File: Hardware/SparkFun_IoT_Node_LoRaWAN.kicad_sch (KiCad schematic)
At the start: 72 parts, among them J1 USB_C_Receptacle, J2 JST_2mm_LiPo, J3 Qwiic_RA, SW1 SMD_4.6x2.8mm_h2.5mm, SW2 SMD_4.6x2.8mm_h2.5mm, U4 W25Q128JVPIM, U5 RT9080-3.3, U6 MCP73831, U7 MAX17048, U8 LM66200, U9 RT9080-3.3

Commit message: v01 schematic updates
Add remaining schematic components
Split schematic into multiple sheets
Still need to define pinouts for RP2350, XBLR, and headers
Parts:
- removed C1, C2, C3, C4, C6, C7: 2.2uF, SparkFun-Capacitor:C_0603_1608Metric, symbol SparkFun-Capacitor:2.2uF_0603_10V_20%
- removed C10, C11, C12, C13, C14, C15, C16, C17, C19, C20, C21, C5, C8, C9: 0.1uF, SparkFun-Capacitor:C_0603_1608Metric, symbol SparkFun-Capacitor:0.1uF_0603_25V_20%
- removed C18, C22: 10uF, SparkFun-Capacitor:C_0603_1608Metric, symbol SparkFun-Capacitor:10uF_0603_6.3V_20%
- removed D1: Yellow, SparkFun-LED:LED_0603_1608Metric, symbol SparkFun-LED:LED_Yellow_0603
- removed D2: WS2812B, SparkFun-LED:WS2812-2020, symbol SparkFun-LED:WS2812B_2020
- removed D3: Red, SparkFun-LED:LED_0603_1608Metric, symbol SparkFun-LED:LED_Red_0603
- removed D4: DT1042-04SO, SparkFun-Semiconductor-Standard:SOT23-6, symbol SparkFun-DiscreteSemi:D_TVS_ESD_USB
- removed J1: USB_C_Receptacle, SparkFun-Connector:USB-C_16, symbol SparkFun-Connector:USB_C_Receptacle
- removed J2: JST_2mm_LiPo, SparkFun-Connector:JST_SMD_2.0mm-2, symbol SparkFun-Connector:Conn_01x02_JST_2mm_LiPo
- removed J3: Qwiic_RA, SparkFun-Connector:JST_SMD_1.0mm-4_RA, symbol SparkFun-Connector:Qwiic_Right_Angle
- removed JP1, JP2, JP4: ~, SparkFun-Jumper:Jumper_2_NC_Trace, symbol SparkFun-Jumper:SolderJumper_2_Bridged
- removed JP3: ~, SparkFun-Jumper:Jumper_3_NC-2_Trace, symbol SparkFun-Jumper:SolderJumper_3_Bridged123
- removed L1: 4.7uH, SparkFun-Coil:1008_2520Metric, symbol SparkFun-Coil:4.7uH_1008_1.4A
- removed R1, R2: 5.1k, SparkFun-Resistor:R_0603_1608Metric, symbol SparkFun-Resistor:5.1k_0603
- removed R10, R9: 2.2k, SparkFun-Resistor:R_0603_1608Metric, symbol SparkFun-Resistor:2.2k_0603
- removed R11, R5, R6, R7: 100k, SparkFun-Resistor:R_0603_1608Metric, symbol SparkFun-Resistor:100k_0603
- removed R12, R14, R16: 10k, SparkFun-Resistor:R_0603_1608Metric, symbol SparkFun-Resistor:10k_0603
- removed R13, R8: 4.7k, SparkFun-Resistor:R_0603_1608Metric, symbol SparkFun-Resistor:4.7k_0603
- removed R15: 1k, SparkFun-Resistor:R_0603_1608Metric, symbol SparkFun-Resistor:1k_0603
- removed R3, R4: 27, SparkFun-Resistor:R_0603_1608Metric, symbol SparkFun-Resistor:27_0603
- removed SW1, SW2: SMD_4.6x2.8mm_h2.5mm, SparkFun-Switch:Push_SMD_4.6x2.8mm, symbol SparkFun-Switch:SPST_Push_SMD_4.6x2.8mm_h2.5mm
- removed U1: ~, RP2350A:RP2350A, symbol RP2350A:RP2350A
- removed U2: ~, RP2350A:APS6404L-3SQR-ZR, symbol RP2350A:APS6404L-3SQR-ZR
- removed U3: ~, SparkFun_IoT_Node_LoRaWAN:XBee_LR, symbol SparkFun_IoT_Node_LoRaWAN:XBee_LR
- removed U4: W25Q128JVPIM, SparkFun-Semiconductor-Standard:WDFN-8_6x5mm-SkinnyCenterPad, symbol SparkFun-IC-Memory:W25Q128JVPIM
- removed U5, U9: RT9080-3.3, SparkFun-Semiconductor-Standard:SOT23-5, symbol SparkFun-Regulator:RT9080-3.3
- removed U6: MCP73831, SparkFun-Semiconductor-Standard:SOT23-5, symbol SparkFun-IC-Power:MCP73831
- removed U7: MAX17048, SparkFun-Semiconductor-Standard:DFN-8, symbol SparkFun-IC-Power:MAX17048
- removed U8: LM66200, SparkFun-Semiconductor-Standard:SOT-583-8, symbol SparkFun-IC-Power:LM66200
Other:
- added sheet Power and Peripherals (power_peripherals.kicad_sch)
- added sheet RP2350 (rp2350.kicad_sch)
- added sheet XBLR (xblr.kicad_sch)
- note removed: "16MB Flash"
- note removed: "8MB PSRAM"
- note removed: "Battery Charger"
- note removed: "Battery Fuel Gauge"
- note removed: "Buttons"
- note removed: "LEDs"
- note removed: "LoRaWAN Module - XBee LR"
- note removed: "Max input voltage: 6V"
- note removed: "PTH Headers"
- note removed: "Peripheral Power Control"
- note removed: "Power Input and Voltage Regulator"
- note removed: "Qwiic Connector"
- note removed: "RP2350"
- note removed: "TODO"
- note removed: "USB-C Connector"

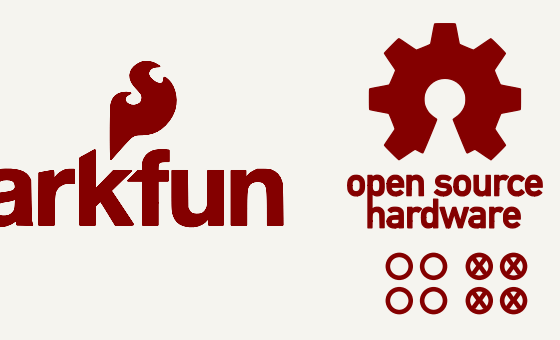
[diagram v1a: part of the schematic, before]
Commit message: Initial board layout
Board outline determined based off selected enclosure
Clusters of components placed and routed
Waiting for feedback before finishing routing
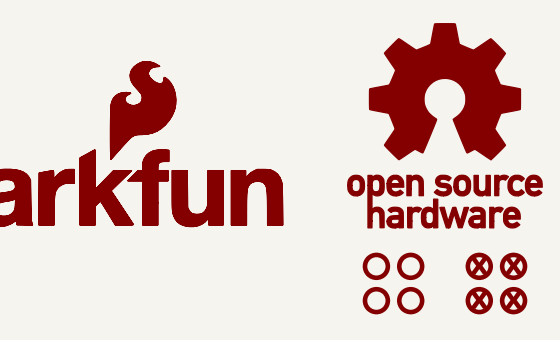
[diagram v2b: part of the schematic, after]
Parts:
- ST1, ST2, ST3, ST4: value Stand_off -> Standoff
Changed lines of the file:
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@@
-	)
-	(symbol
-		(lib_id "SparkFun-Hardware:Standoff")
-		(at 250.19 179.07 0)
-		(unit 1)
-		(exclude_from_sim no)
-		(in_bom yes)
-		(on_board yes)
-		(dnp no)
-		(property "Reference" "ST2"
-			(at 250.19 176.53 0)
-			(effects
-				(font
-					(size 1.27 1.27)
-				)
-				(hide yes)
-			)
-		)
-		(property "Value" "Stand_off"
-			(at 250.19 181.61 0)
-			(effects
-				(font
-					(size 1.27 1.27)
-				)
-				(hide yes)
-			)
-		)
-		(property "Footprint" "SparkFun-Hardware:Standoff"
-			(at 250.19 184.15 0)
-			(effects
-				(font
-					(size 1.27 1.27)
-				)
-				(hide yes)
-			)
-		)
-		(property "Datasheet" "~"
-			(at 250.19 182.88 0)
-			(effects
-				(font
-					(size 1.27 1.27)
-				)
-				(hide yes)
-			)
-		)
-		(property "Description" ""
-			(at 250.19 179.07 0)
-			(effects
-				(font
-					(size 1.27 1.27)
-				)
-				(hide yes)
-			)
-		)
-		(instances
-			(project "SparkFun_Default_KiCad_Setup"
-				(path "/e3dd3ae4-244d-4cba-9cca-5d2abf83f29a"
-					(reference "ST2")
-					(unit 1)
-				)
-			)
-		)
 	)
 	(symbol
@@
 	(symbol
 		(lib_id "SparkFun-Hardware:Standoff")
-		(at 254 179.07 0)
-		(unit 1)
-		(exclude_from_sim no)
-		(in_bom yes)
-		(on_board yes)
-		(dnp no)
+		(at 247.65 175.26 0)
+		(unit 1)
+		(exclude_from_sim no)
+		(in_bom yes)
+		(on_board yes)
+		(dnp no)
+		(fields_autoplaced yes)
 		(property "Reference" "ST4"
-			(at 254 176.53 0)
-			(effects
-				(font
-					(size 1.27 1.27)
-				)
-				(hide yes)
-			)
-		)
-		(property "Value" "Stand_off"
-			(at 254 181.61 0)
+			(at 247.65 172.72 0)
+			(effects
+				(font
+					(size 1.27 1.27)
+				)
+				(hide yes)
+			)
+		)
+		(property "Value" "Standoff"
+			(at 247.65 177.8 0)
 			(effects
 				(font
@@
 		)
 		(property "Footprint" "SparkFun-Hardware:Standoff"
-			(at 254 184.15 0)
-			(effects
-				(font
-					(size 1.27 1.27)
-				)
-				(hide yes)
-			)
-		)
-		(property "Datasheet" "~"
-			(at 254 182.88 0)
-			(effects
-				(font
-					(size 1.27 1.27)
-				)
-				(hide yes)
-			)
-		)
-		(property "Description" ""
-			(at 254 179.07 0)
-			(effects
-				(font
-					(size 1.27 1.27)
-				)
-				(hide yes)
-			)
-		)
-		(instances
-			(project "SparkFun_Default_KiCad_Setup"
+			(at 247.65 180.34 0)
+			(effects
+				(font
+					(size 1.27 1.27)
+				)
+				(hide yes)
+			)
+		)
+		(property "Datasheet" "~"
+			(at 247.65 179.07 0)
+			(effects
+				(font
+					(size 1.27 1.27)
+				)
+				(hide yes)
+			)
+		)
+		(property "Description" "Drill holes for mechanically mounting via screws, standoffs, etc."
+			(at 247.65 175.26 0)
+			(effects
+				(font
+					(size 1.27 1.27)
+				)
+				(hide yes)
+			)
+		)
+		(instances
+			(project "SparkFun_IoT_Node_LoRaWAN"
 				(path "/e3dd3ae4-244d-4cba-9cca-5d2abf83f29a"
 					(reference "ST4")
@@
 	(symbol
 		(lib_id "SparkFun-Hardware:Standoff")
-		(at 250.19 175.26 0)
-		(unit 1)
-		(exclude_from_sim no)
-		(in_bom yes)
-		(on_board yes)
-		(dnp no)
+		(at 247.65 179.07 0)
+		(unit 1)
+		(exclude_from_sim no)
+		(in_bom yes)
+		(on_board yes)
+		(dnp no)
+		(fields_autoplaced yes)
+		(property "Reference" "ST3"
+			(at 247.65 176.53 0)
+			(effects
+				(font
+					(size 1.27 1.27)
+				)
+				(hide yes)
+			)
+		)
+		(property "Value" "Standoff"
+			(at 247.65 181.61 0)
+			(effects
+				(font
+					(size 1.27 1.27)
+				)
+				(hide yes)
+			)
+		)
+		(property "Footprint" "SparkFun-Hardware:Standoff"
+			(at 247.65 184.15 0)
+			(effects
+				(font
+					(size 1.27 1.27)
+				)
+				(hide yes)
+			)
+		)
+		(property "Datasheet" "~"
+			(at 247.65 182.88 0)
+			(effects
+				(font
+					(size 1.27 1.27)
+				)
+				(hide yes)
+			)
+		)
+		(property "Description" "Drill holes for mechanically mounting via screws, standoffs, etc."
+			(at 247.65 179.07 0)
+			(effects
+				(font
+					(size 1.27 1.27)
+				)
+				(hide yes)
+			)
+		)
+		(instances
+			(project "SparkFun_IoT_Node_LoRaWAN"
+				(path "/e3dd3ae4-244d-4cba-9cca-5d2abf83f29a"
+					(reference "ST3")
+					(unit 1)
+				)
+			)
+		)
+	)
+	(symbol
+		(lib_id "SparkFun-Hardware:Standoff")
+		(at 251.46 179.07 0)
+		(unit 1)
+		(exclude_from_sim no)
+		(in_bom yes)
+		(on_board yes)
+		(dnp no)
+		(fields_autoplaced yes)
+		(property "Reference" "ST2"
+			(at 251.46 176.53 0)
+			(effects
+				(font
+					(size 1.27 1.27)
+				)
+				(hide yes)
+			)
+		)
+		(property "Value" "Standoff"
+			(at 251.46 181.61 0)
+			(effects
+				(font
+					(size 1.27 1.27)
+				)
+				(hide yes)
+			)
+		)
+		(property "Footprint" "SparkFun-Hardware:Standoff"
+			(at 251.46 184.15 0)
+			(effects
+				(font
+					(size 1.27 1.27)
+				)
+				(hide yes)
+			)
+		)
+		(property "Datasheet" "~"
+			(at 251.46 182.88 0)
+			(effects
+				(font
+					(size 1.27 1.27)
+				)
+				(hide yes)
+			)
+		)
+		(property "Description" "Drill holes for mechanically mounting via screws, standoffs, etc."
+			(at 251.46 179.07 0)
+			(effects
+				(font
+					(size 1.27 1.27)
+				)
+				(hide yes)
+			)
+		)
+		(instances
+			(project "SparkFun_IoT_Node_LoRaWAN"
+				(path "/e3dd3ae4-244d-4cba-9cca-5d2abf83f29a"
+					(reference "ST2")
+					(unit 1)
+				)
+			)
+		)
+	)
+	(symbol
+		(lib_id "SparkFun-Hardware:Standoff")
+		(at 251.46 175.26 0)
+		(unit 1)
+		(exclude_from_sim no)
+		(in_bom yes)
+		(on_board yes)
+		(dnp no)
+		(fields_autoplaced yes)
 		(property "Reference" "ST1"
-			(at 250.19 172.72 0)
-			(effects
-				(font
-					(size 1.27 1.27)
-				)
-				(hide yes)
-			)
-		)
-		(property "Value" "Stand_off"
-			(at 250.19 177.8 0)
+			(at 251.46 172.72 0)
+			(effects
+				(font
+					(size 1.27 1.27)
+				)
+				(hide yes)
+			)
+		)
+		(property "Value" "Standoff"
+			(at 251.46 177.8 0)
 			(effects
 				(font
@@
 		)
 		(property "Footprint" "SparkFun-Hardware:Standoff"
-			(at 250.19 180.34 0)
-			(effects
-				(font
-					(size 1.27 1.27)
-				)
-				(hide yes)
-			)
-		)
-		(property "Datasheet" "~"
-			(at 250.19 179.07 0)
-			(effects
-				(font
-					(size 1.27 1.27)
-				)
-				(hide yes)
-			)
-		)
-		(property "Description" ""
-			(at 250.19 175.26 0)
-			(effects
-				(font
-					(size 1.27 1.27)
-				)
-				(hide yes)
-			)
-		)
-		(instances
-			(project "SparkFun_Default_KiCad_Setup"
+			(at 251.46 180.34 0)
+			(effects
+				(font
+					(size 1.27 1.27)
+				)
+				(hide yes)
+			)
+		)
+		(property "Datasheet" "~"
+			(at 251.46 179.07 0)
+			(effects
+				(font
+					(size 1.27 1.27)
+				)
+				(hide yes)
+			)
+		)
+		(property "Description" "Drill holes for mechanically mounting via screws, standoffs, etc."
+			(at 251.46 175.26 0)
+			(effects
+				(font
+					(size 1.27 1.27)
+				)
+				(hide yes)
+			)
+		)
+		(instances
+			(project ""
 				(path "/e3dd3ae4-244d-4cba-9cca-5d2abf83f29a"
 					(reference "ST1")
@@
 					(unit 1)
 				)
-			)
-		)
-	)
-	(symbol
-		(lib_id "SparkFun-Hardware:Standoff")
-		(at 254 175.26 0)
-		(unit 1)
-		(exclude_from_sim no)
-		(in_bom yes)
-		(on_board yes)
-		(dnp no)
-		(fields_autoplaced yes)
-		(property "Reference" "ST3"
-			(at 254 172.72 0)
-			(effects
-				(font
-					(size 1.27 1.27)
-				)
-				(hide yes)
-			)
-		)
-		(property "Value" "Stand_off"
-			(at 254 177.8 0)
-			(effects
-				(font
-					(size 1.27 1.27)
-				)
-				(hide yes)
-			)
-		)
-		(property "Footprint" "SparkFun-Hardware:Standoff"
-			(at 254 180.34 0)
-			(effects
-				(font
-					(size 1.27 1.27)
-				)
-				(hide yes)
-			)
-		)
-		(property "Datasheet" "~"
-			(at 254 179.07 0)
-			(effects
-				(font
-					(size 1.27 1.27)
-				)
-				(hide yes)
-			)
-		)
-		(property "Description" ""
-			(at 254 175.26 0)
-			(effects
-				(font
-					(size 1.27 1.27)
-				)
-				(hide yes)
-			)
-		)
-		(instances
-			(project "SparkFun_Default_KiCad_Setup"
-				(path "/e3dd3ae4-244d-4cba-9cca-5d2abf83f29a"
-					(reference "ST3")
-					(unit 1)
-				)

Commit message: v02 Schematic Updates
Bump version number to v02
Fix RP2350, APS6404L, and 12MHz crystal to use proper KiCad symbols and footprints instead of imported from Eagle
Change schematic to use 2x Ledger sheets
Change Qwiic connector to power from 3.3V
Change user button and RGB LED to small mount versions
Split headers into XBLR and IoT Node specific regions
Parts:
- added C10, C11, C12, C13, C14, C15, C16, C17, C19, C21, C22, C27, C31, C9: 0.1uF, SparkFun-Capacitor:C_0603_1608Metric, symbol SparkFun-Capacitor:0.1uF_0603_25V_20%
- added C18, C20, C23: 10uF, SparkFun-Capacitor:C_0603_1608Metric, symbol SparkFun-Capacitor:10uF_0603_6.3V_20%
- added C24: 1.0uF, SparkFun-Capacitor:C_0603_1608Metric, symbol SparkFun-Capacitor:1.0uF_0603_16V_10%
- added C25: 10pF, SparkFun-Capacitor:C_0603_1608Metric, symbol SparkFun-Capacitor:10pF_0603_50V_5%
- added C28: 2.2uF, SparkFun-Capacitor:C_0603_1608Metric, symbol SparkFun-Capacitor:2.2uF_0603_10V_20%
- added C29, C30: 15pF, SparkFun-Capacitor:C_0603_1608Metric, symbol SparkFun-Capacitor:15pF_0603_50V_5%
- added D4, D5: DT1042-04SO, SparkFun-Semiconductor-Standard:SOT23-6, symbol SparkFun-DiscreteSemi:D_TVS_ESD_USB
- added D6: BAT20J, SparkFun-Semiconductor-Standard:SOD-323, symbol SparkFun-DiscreteSemi:D_Schottky_1A_23V_0.62V
- added J1: Conn_01x03, SparkFun-Connector:1x03, symbol SparkFun-Connector:Conn_01x03
- added J4, J5: USB_C_Receptacle, SparkFun-Connector:USB-C_16, symbol SparkFun-Connector:USB_C_Receptacle
- added J6: SWD, SparkFun-Connector:2x5_1.27mm_SMD_Unshrouded, symbol SparkFun-Connector:Debug-Cortex-2x5-SMD-Unshrouded
- added JP1, JP5: ~, SparkFun-Jumper:Jumper_2_NC_Trace, symbol SparkFun-Jumper:SolderJumper_2_Bridged
- added JP6: Measure, SparkFun-Jumper:Jumper_2_PTH_SMD_Combo-NC, symbol SparkFun-Jumper:Jumper_Measure
- added L1: 4.7uH, SparkFun-Coil:1008_2520Metric, symbol SparkFun-Coil:4.7uH_1008_1.4A
- added R1, R17, R18, R2, R29: 5.1k, SparkFun-Resistor:R_0603_1608Metric, symbol SparkFun-Resistor:5.1k_0603
- added R12, R14, R16, R21, R22, R30: 10k, SparkFun-Resistor:R_0603_1608Metric, symbol SparkFun-Resistor:10k_0603
- added R15, R25: 1k, SparkFun-Resistor:R_0603_1608Metric, symbol SparkFun-Resistor:1k_0603
- added R23: 10, SparkFun-Resistor:R_0603_1608Metric, symbol SparkFun-Resistor:10_0603
- added R3, R4: 27, SparkFun-Resistor:R_0603_1608Metric, symbol SparkFun-Resistor:27_0603
- added SW1, SW2, SW4: SMD_4.6x2.8mm_h2.5mm, SparkFun-Switch:Push_SMD_4.6x2.8mm, symbol SparkFun-Switch:SPST_Push_SMD_4.6x2.8mm_h2.5mm
- added SW3: DPDT_Slide_SMD_7.2x3.5mm, SparkFun-Switch:Slide_DPDT_SMD_7.2x3.5mm, symbol SparkFun-Switch:DPDT_Slide_SMD_7.2x3.5mm
- added U1: RP2350A, SparkFun_IoT_Node_LoRaWAN:RP2350A, symbol SparkFun_IoT_Node_LoRaWAN:RP2350A
- added U10: XBLR, SparkFun_IoT_Node_LoRaWAN:XBee_LR, symbol SparkFun_IoT_Node_LoRaWAN:XBee_LR
- added U2: APS6404L-3SQR-ZR, SparkFun-Semiconductor-Standard:USON-8_3x2mm-SkinnyCenterPad, symbol SparkFun-IC-Memory:APS6404L-3SQR-ZR
- added U3: CH340C, SparkFun-Semiconductor-Standard:SO-16, symbol SparkFun-IC-Comm:CH340C
- added U4: W25Q128JVPIM, SparkFun-Semiconductor-Standard:WDFN-8_6x5mm-SkinnyCenterPad, symbol SparkFun-IC-Memory:W25Q128JVPIM
- added Y1: 12MHz, SparkFun-Clock:Crystal_SMD_2.5x2.0mm, symbol SparkFun-Clock:Crystal_12MHz_2.5x2.0mm
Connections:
- new net: J4.A5 (CC1), R18.1
- new net: J4.A8 (NC), J4.B8 (NC)
- new net: J4.B5 (CC2), R17.1
- new net: J4.NC1 (NC), J4.NC2 (NC), J4.NC3 (NC)
- new net: J4.S (SHIELD), JP5.1 (A)
- new net: J5.A5 (CC1), R2.1
- new net: J5.A8 (NC), J5.B8 (NC)
- new net: J5.B5 (CC2), R1.1
- new net: J5.NC1 (NC), J5.NC2 (NC), J5.NC3 (NC)
- new net: J5.S (SHIELD), JP1.1 (A)
- new net: R25.1, U1.22 (XOUT)
- new net: C29.2, R25.2, Y1.1
- new net: C30.2, U1.21 (XIN), Y1.3
- new net: R29.1, U3.2 (TXD)
- new net: L1.2, U1.48 (VREG_LX)
- new net 1.1V: C12.1, C14.1, C16.1, C18.1, L1.1, U1.23 (DVDD), U1.39 (DVDD), U1.50 (VREG_FB), U1.6 (DVDD)
- new net 3.3V: C10.1, C11.1, C13.1, C15.1, C17.1, C19.1, C20.1, C21.1, C22.1, C9.1, J6.1 (VCC), JP6.1 (A), R12.1, R14.1, R16.1, R21.1, R22.1, R23.2, U1.1 (IOVDD), U1.11 (IOVDD), U1.20 (IOVDD), U1.30 (IOVDD), U1.38 (IOVDD), U1.45 (IOVDD), U1.49 (VREG_VIN), U1.53 (USB_OTP_VDD), U1.54 (QSPI_IOVDD), U2.8 (VCC), U4.8 (VCC)
- new net 3.3V_XBLR: C23.1, C24.1, C25.1, JP6.2 (B), U10.2 (VCC)
- new net BAT_POWER: U1.34 (GPIO22)
- new net FUEL_GAUGE_~{ALRT}: U1.35 (GPIO23)
- new net GND: C10.2, C11.2, C12.2, C13.2, C14.2, C15.2, C16.2, C17.2, C18.2, C19.2, C20.2, C21.2, C22.2, C23.2, C24.2, C25.2, C27.2, C28.2, C29.1, C30.1, C31.2, C9.2, D4.2 (GND), D5.2 (GND), J1.2 (Pin_2), J4.GND, J5.GND, J6.3 (GND), J6.5 (GND), J6.9 (GND), JP1.2 (B), JP5.2 (B), R1.2, R17.2, R18.2, R2.2, R30.2, SW1.1, SW2.1, SW4.1, U1.47 (VREG_PGND), U1.EPAD (GND), U10.1 (GND), U10.10 (GND), U10.12 (GND), U10.21 (GND), U10.32 (GND), U10.34 (GND), U2.4 (GND), U2.9 (GND), U3.1 (GND), U4.4 (GND), Y1.2, Y1.4
- new net LED_IN: U1.37 (GPIO25)
- new net PERIPHERAL_POWER: U1.9 (GPIO6)
- new net PSRAM_~{CS}: R12.2, U1.12 (GPIO8), U2.1 (~{CS})
- new net QSPI_D0: U1.57 (QSPI_SD0), U2.5 (D0/DI), U4.5 (D0/DI)
- new net QSPI_D1: U1.59 (QSPI_SD1), U2.2 (D1/DO), U4.2 (D1/DO)
- new net QSPI_D2: U1.58 (QSPI_SD2), U2.3 (D2/~{WP}), U4.3 (D2/~{WP})
- new net QSPI_D3: U1.55 (QSPI_SD3), U2.7 (D3/~{HOLD}), U4.7 (D3/~{HOLD})
- new net QSPI_SCLK: U1.56 (QSPI_SCLK), U2.6 (CLK), U4.6 (CLK)
- new net QSPI_~{CS}: R15.2, R16.2, U1.60 (QSPI_~{CS}), U4.1 (~{CS})
- new net RP2350_IO10: U1.14 (GPIO10)
- new net RP2350_IO11: U1.15 (GPIO11)
- new net RP2350_IO12: U1.16 (GPIO12)
- new net RP2350_IO13: U1.17 (GPIO13)
- new net RP2350_IO14: U1.18 (GPIO14)
- new net RP2350_IO15: U1.19 (GPIO15)
- new net RP2350_IO16: U1.27 (GPIO16)
- new net RP2350_IO17: U1.28 (GPIO17)
- new net RP2350_IO20: U1.32 (GPIO20)
- new net RP2350_IO21: U1.33 (GPIO21)
- new net RP2350_IO26: U1.40 (GPIO26/ADC0)
- new net RP2350_IO27: U1.41 (GPIO27/ADC1)
- new net RP2350_IO28: U1.42 (GPIO28/ADC2)
- new net RP2350_IO29: U1.43 (GPIO29/ADC3)
- new net RP2350_IO9: U1.13 (GPIO9)
- new net RP2350_RX: SW3.4 (A), U1.31 (GPIO19)
- new net RP2350_SWCLK: J1.1 (Pin_1), U1.24 (SWCLK)
- new net RP2350_SWDIO: J1.3 (Pin_3), U1.25 (SWDIO)
- new net RP2350_TX: SW3.1 (A), U1.29 (GPIO18)
- new net RP2350_USB_D+: R3.1, U1.52 (USB_D+)
- new net RP2350_USB_D-: R4.1, U1.51 (USB_D-)
- new net SCL: U1.8 (GPIO5)
- new net SDA: U1.7 (GPIO4)
- new net SD_DET: U1.10 (GPIO7)
- new net SD_PICO: U1.5 (GPIO3)
- new net SD_POCI: U1.2 (GPIO0)
- new net SD_SCK: U1.4 (GPIO2)
- new net SD_~{CS}: U1.3 (GPIO1)
- new net USB_D+: D4.3 (I/O2), D4.4 (I/O3), J5.A6 (D+), J5.B6 (D+), R3.2
- new net USB_D-: D4.1 (I/O1), D4.6 (I/O4), J5.A7 (D-), J5.B7 (D-), R4.2
- new net USER_BUTTON: R21.2, SW4.2, U1.36 (GPIO24)
- new net V3: C27.1, U3.4 (V3)
- new net VDDA: C28.1, R23.1, U1.44 (ADC_IOVDD), U1.46 (VREG_AVDD)
- new net VUSB: D4.5 (VCC), D6.C, J5.VBUS
- new net VUSB_2: C31.1, D5.5 (VCC), D6.A, J4.VBUS, U3.16 (VCC)
- new net XBLR_IO0: U10.31 (COMM/AD0/DIO0)
- new net XBLR_IO1: U10.30 (AD1/DIO1)
- new net XBLR_IO10: U10.7 (PWM0/RSSI/DIO10)
- new net XBLR_IO11: U10.8 (PWM1/DIO11)
- new net XBLR_IO12: U10.5 (DIO12)
- new net XBLR_IO15: U10.16 (SPI_MISO/DIO15)
- new net XBLR_IO16: U10.15 (SPI_MOSI/DIO16)
- new net XBLR_IO17: U10.14 (SPI_~{SSEL}/DIO17)
- new net XBLR_IO18: U10.13 (SPI_SCLK/DIO18)
- new net XBLR_IO19: U10.11 (~{ATTN}/DIO19)
- new net XBLR_IO2: U10.29 (AD2/DIO2)
- new net XBLR_IO3: U10.28 (AD3/DIO3)
- new net XBLR_IO4: U10.23 (DIO4)
- new net XBLR_IO5: U10.26 (ASSOC/DIO5)
- new net XBLR_IO6: U10.27 (~{RTS}/DIO6)
- new net XBLR_IO7: U10.24 (~{CTS}/DIO7)
- new net XBLR_IO8: U10.9 (~{DTR}/DIO8)
- new net XBLR_IO9: U10.25 (ON/~{SLP}/DIO9)
- new net XBLR_RX/IO14: SW3.2 (B), U10.4 (DIN/~{CONFIG}/DIO14)
- new net XBLR_SWCLK: J6.4 (SWDCLK), U10.17 (JTCK/SWCLK_0)
- new net XBLR_SWDIO: J6.2 (SWDIO), U10.20 (JTMS/SWDIO_0)
- new net XBLR_SWO: J6.6 (SWO), U10.18 (JTDO/SWO_0)
- new net XBLR_TX/IO13: SW3.5 (B), U10.3 (DOUT/DIO13)
- new net XBLR_USB_D+: D5.3 (I/O2), D5.4 (I/O3), J4.A6 (D+), J4.B6 (D+), U3.5 (UD+)
- new net XBLR_USB_D-: D5.1 (I/O1), D5.6 (I/O4), J4.A7 (D-), J4.B7 (D-), U3.6 (UD-)
- new net XBLR_USB_RX: SW3.6 (C), U3.3 (RXD)
- new net XBLR_USB_TX: R29.2, R30.1, SW3.3 (C)
- new net XBLR_~{RESET}: J6.10 (~{RESET}), R22.2, U10.6 (~{RESET})
- new net ~{BOOT}: R15.1, SW1.2
- new net ~{RESET}: R14.2, SW2.2, U1.26 (RUN)
- no-connect marks 0 -> 10
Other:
- removed sheet RP2350
- removed sheet XBLR
- note added: "16MB Flash - W25Q128JVPIM"
- note added: "8MB PSRAM - APS6404L"
- note added: "Buttons"
- note added: "Cut MEAS trace to measure current consumed by XBLR"
- note added: "Cut SHLD trace to disconnect USB shield from GND"
- note added: "LoRaWAN Module - XBee LR"
- note added: "Power and Peripherals"
- note added: "RP2350"
- note added: "RP2350 Debug Header"
- note added: "RP2350 USB-C Connector"
- note added: "XBLR Debug Header"
- note added: "XBLR UART Selection"
- note added: "XBLR USB to UART Converter - CH340"
- note added: "XBLR USB-C Connector"
- company: (none) -> SparkFun

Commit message: Finish v02 updates
Clean up schematic
Add test points for boot button and RGB LED output
Update pinouts of headers and RP2350
Fix pad shape of XBLR footprint
Finish routing
Update logos
Update jumper names
Add measures
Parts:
- removed R14, R21: 10k, SparkFun-Resistor:R_0603_1608Metric, symbol SparkFun-Resistor:10k_0603
- removed SW1, SW2, SW4: SMD_4.6x2.8mm_h2.5mm, SparkFun-Switch:Push_SMD_4.6x2.8mm, symbol SparkFun-Switch:SPST_Push_SMD_4.6x2.8mm_h2.5mm
- added C8: 1.0uF, SparkFun-Capacitor:C_0603_1608Metric, symbol SparkFun-Capacitor:1.0uF_0603_16V_10%
- added G4: qwiic_Logo, symbol SparkFun-Aesthetic:qwiic_Logo
- JP1: value ~ -> SHLD
- JP5: value ~ -> XB_SHLD
- JP6: value Measure -> XB_MEAS
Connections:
- net RP2350_IO12 is gone; now on net SD_POCI: U1.16 (GPIO12)
- net RP2350_IO13 is gone; now on net SD_~{CS}: U1.17 (GPIO13)
- net RP2350_IO14 is gone; now on net SD_SCK: U1.18 (GPIO14)
- net RP2350_IO15 is gone; now on net SD_PICO: U1.19 (GPIO15)
- net RP2350_IO16 is gone; now on net PERIPHERAL_POWER: U1.27 (GPIO16)
- net RP2350_IO17 is gone; now on net SD_DET: U1.28 (GPIO17)
- net RP2350_IO20 is gone; now on net SDA: U1.32 (GPIO20)
- net RP2350_IO21 is gone; now on net SCL: U1.33 (GPIO21)
- net 3.3V: now also C8.1
- net GND: now also C8.2
- net PERIPHERAL_POWER: no longer U1.9 (GPIO6)
- net PSRAM_~{CS}: now also U1.2 (GPIO0); no longer U1.12 (GPIO8)
- net SCL: no longer U1.8 (GPIO5)
- net SDA: no longer U1.7 (GPIO4)
- net SD_DET: no longer U1.10 (GPIO7)
- net SD_PICO: no longer U1.5 (GPIO3)
- net SD_POCI: no longer U1.2 (GPIO0)
- net SD_SCK: no longer U1.4 (GPIO2)
- net SD_~{CS}: no longer U1.3 (GPIO1)
- new net RP2350_IO1: U1.3 (GPIO1)
- new net RP2350_IO2: U1.4 (GPIO2)
- new net RP2350_IO3: U1.5 (GPIO3)
- new net RP2350_IO4: U1.7 (GPIO4)
- new net RP2350_IO5: U1.8 (GPIO5)
- new net RP2350_IO6: U1.9 (GPIO6)
- new net RP2350_IO7: U1.10 (GPIO7)
- new net RP2350_IO8: U1.12 (GPIO8)
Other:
- note added: "Cut XB_MEAS trace to measure current consumed by XBLR"
- note added: "Cut XB_SHLD trace to disconnect USB shield from GND"
- note added: "Differential pair calculation: Conducto Width: 0.2326mm Conductor Spacing 0.127mm Height: 0.2104mm Dielectric Constant: 4.6 Impedance: 89.999 Ohms Computed with Saturn PCB Toolkit"
- note removed: "Buttons"
- note removed: "Cut MEAS trace to measure current consumed by XBLR"
- moved on the sheet: C21, C22, D4, J5, R1, R12, R15, R16, R2, R3, R4, U2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

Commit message: Re-annotate schematic
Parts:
- renumbered C9 to C1, C17 to C10, C14 to C11, C19 to C12, C16 to C13, C20 to C14, C18 to C15, C8 to C16, C22 to C17, C21 to C18, C31 to C19, C30 to C2, C23 to C20, C27 to C21, C24 to C22, C25 to C23, C10 to C3, C28 to C4, C29 to C5, C11 to C6, C13 to C7, C15 to C8, C12 to C9, D4 to D1, D6 to D2, D5 to D3, G4 to G1, G1 to G2, G2 to G3, G3 to G4, J5 to J1, J1 to J2, J4 to J3, J6 to J4, JP6 to JP2, JP5 to JP3, R23 to R1, R22 to R10, R17 to R11, R18 to R12, R29 to R13, R30 to R14, R25 to R2, R1 to R3, R2 to R4, R3 to R5, R4 to R6, R15 to R7, R12 to R8, R16 to R9, ST4 to ST1, ST3 to ST2, ST1 to ST3, ST2 to ST4, SW3 to SW1, U4 to U2, U2 to U3, U10 to U4, U3 to U5
